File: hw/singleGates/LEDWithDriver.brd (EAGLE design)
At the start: 3 parts, among them Q1 BC817

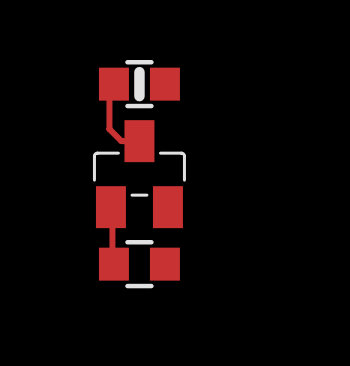
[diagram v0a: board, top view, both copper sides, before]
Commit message: Add led output and prepare first alu slice
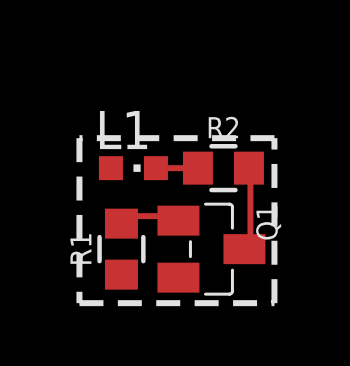
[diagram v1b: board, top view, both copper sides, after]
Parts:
- added L1: (no value), p.peter-leds:CHIPLED_0603
- R2: device p.peter-rcl:R0603-MARK -> p.peter-gator:R0603
- moved R2 3.96 mm to (4.80, 4.50), turned to 0 degrees
- moved Q1 3.47 mm to (4.40, 1.80), turned to 270 degrees
- moved R1 0.78 mm to (1.40, 1.80), turned to 90 degrees
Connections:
- net NOT renamed N$1
- new net INT: L1.C, R2.1
- net _VP: now also L1.A; no longer R2.1
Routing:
- net INT: track 0.00 -> 1.40 mm
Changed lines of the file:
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@@
 <layer number="23" name="tOrigins" color="15" fill="1" visible="yes" active="yes"/>
 <layer number="24" name="bOrigins" color="15" fill="1" visible="yes" active="yes"/>
-<layer number="25" name="tNames" color="7" fill="1" visible="yes" active="yes"/>
+<layer number="25" name="tNames" color="7" fill="1" visible="no" active="yes"/>
 <layer number="26" name="bNames" color="7" fill="1" visible="yes" active="yes"/>
-<layer number="27" name="tValues" color="7" fill="1" visible="yes" active="yes"/>
+<layer number="27" name="tValues" color="7" fill="1" visible="no" active="yes"/>
 <layer number="28" name="bValues" color="7" fill="1" visible="yes" active="yes"/>
 <layer number="29" name="tStop" color="7" fill="3" visible="yes" active="yes"/>
@@
 <layer number="107" name="Crop" color="7" fill="1" visible="yes" active="yes"/>
 <layer number="108" name="centerline" color="7" fill="1" visible="yes" active="yes"/>
-<layer number="109" name="fp9" color="7" fill="1" visible="yes" active="yes"/>
-<layer number="110" name="fp0" color="7" fill="1" visible="yes" active="yes"/>
+<layer number="109" name="fp9" color="7" fill="1" visible="no" active="yes"/>
+<layer number="110" name="fp0" color="7" fill="1" visible="no" active="yes"/>
 <layer number="116" name="Patch_BOT" color="9" fill="4" visible="yes" active="yes"/>
 <layer number="121" name="_tsilk" color="7" fill="1" visible="yes" active="yes"/>
 <layer number="122" name="_bsilk" color="7" fill="1" visible="yes" active="yes"/>
-<layer number="123" name="tTestmark" color="7" fill="1" visible="yes" active="yes"/>
-<layer number="124" name="bTestmark" color="7" fill="1" visible="yes" active="yes"/>
+<layer number="123" name="tTestmark" color="7" fill="1" visible="no" active="yes"/>
+<layer number="124" name="bTestmark" color="7" fill="1" visible="no" active="yes"/>
 <layer number="125" name="_tNames" color="7" fill="1" visible="yes" active="yes"/>
 <layer number="131" name="prix" color="7" fill="1" visible="yes" active="yes"/>
@@
 <layer number="144" name="Drill_legend" color="7" fill="1" visible="yes" active="yes"/>
 <layer number="151" name="HeatSink" color="7" fill="1" visible="yes" active="yes"/>
-<layer number="199" name="Contour" color="7" fill="1" visible="yes" active="yes"/>
+<layer number="199" name="Contour" color="7" fill="1" visible="no" active="yes"/>
 <layer number="200" name="200bmp" color="1" fill="10" visible="no" active="no"/>
 <layer number="201" name="201bmp" color="2" fill="10" visible="yes" active="yes"/>
@@
 <board>
 <plain>
-<wire x1="0" y1="8.5" x2="4" y2="8.5" width="0.2" layer="22" style="shortdash"/>
-<wire x1="4" y1="8.5" x2="4" y2="0" width="0.2" layer="22" style="shortdash"/>
-<wire x1="4" y1="0" x2="0" y2="0" width="0.2" layer="22" style="shortdash"/>
-<wire x1="0" y1="0" x2="0" y2="8.5" width="0.2" layer="22" style="shortdash"/>
+<wire x1="0" y1="0" x2="6.5" y2="0" width="0.2" layer="21" style="shortdash"/>
+<wire x1="6.5" y1="0" x2="6.5" y2="5.5" width="0.2" layer="21" style="shortdash"/>
+<wire x1="6.5" y1="5.5" x2="0" y2="5.5" width="0.2" layer="21" style="shortdash"/>
+<wire x1="0" y1="5.5" x2="0" y2="0" width="0.2" layer="21" style="shortdash"/>
 </plain>
 <attributes>
@@
 </autorouter>
 <elements>
-<element name="R1" library="p.peter-gator" package="R0603" value="10k" x="2" y="1.3" smashed="yes" rot="R180">
-<attribute name="SV_SPICE_ORDER" value="1;2" x="2" y="1.3" size="1.778" layer="27" rot="R180" display="off"/>
-<attribute name="SV_SPICE_PREFIX" value="R" x="2" y="1.3" size="1.778" layer="27" rot="R180" display="off"/>
+<element name="R1" library="p.peter-gator" package="R0603" value="10k" x="1.4" y="1.8" rot="R90">
+<attribute name="SV_SPICE_ORDER" value="1;2" x="1.4" y="1.8" size="1.778" layer="27" rot="R90" display="off"/>
+<attribute name="SV_SPICE_PREFIX" value="R" x="1.4" y="1.8" size="1.778" layer="27" rot="R90" display="off"/>
 </element>
-<element name="R2" library="p.peter-rcl" package="R0603-MARK" value="1k" x="2" y="7.3" smashed="yes" rot="R180"/>
-<element name="Q1" library="p.peter-gator" package="SOT23" value="BC817" x="2" y="4.3" smashed="yes">
-<attribute name="SV_SPICE_MODEL" value="NPN ()" x="2" y="4.3" size="1.778" layer="27" display="off"/>
-<attribute name="SV_SPICE_ORDER" value="COLLECTOR;BASE;EMITTER" x="2" y="4.3" size="1.778" layer="27" display="off"/>
-<attribute name="SV_SPICE_PREFIX" value="Q" x="2" y="4.3" size="1.778" layer="27" display="off"/>
+<element name="R2" library="p.peter-gator" package="R0603" value="1k" x="4.8" y="4.5">
+<attribute name="SV_SPICE_ORDER" value="1;2" x="4.8" y="4.5" size="1.778" layer="27" display="off"/>
+<attribute name="SV_SPICE_PREFIX" value="R" x="4.8" y="4.5" size="1.778" layer="27" display="off"/>
 </element>
+<element name="Q1" library="p.peter-gator" package="SOT23" value="BC817" x="4.4" y="1.8" rot="R270">
+<attribute name="SV_SPICE_MODEL" value="NPN ()" x="4.4" y="1.8" size="1.778" layer="27" rot="R270" display="off"/>
+<attribute name="SV_SPICE_ORDER" value="COLLECTOR;BASE;EMITTER" x="4.4" y="1.8" size="1.778" layer="27" rot="R270" display="off"/>
+<attribute name="SV_SPICE_PREFIX" value="Q" x="4.4" y="1.8" size="1.778" layer="27" rot="R270" display="off"/>
+</element>
+<element name="L1" library="p.peter-leds" package="CHIPLED_0603" value="" x="1.8" y="4.5" rot="R270"/>
 </elements>
 <signals>
 <signal name="_VN">
+<wire x1="3.5" y1="0.65" x2="3.3" y2="0.85" width="0.2" layer="1"/>
 <contactref element="Q1" pad="P$2"/>
 </signal>
-<signal name="N$14">
+<signal name="INT">
+<contactref element="R2" pad="1"/>
+<contactref element="L1" pad="C"/>
+<wire x1="3.95" y1="4.5" x2="2.55" y2="4.5" width="0.2" layer="1"/>
+</signal>
+<signal name="N$16">
 <contactref element="R1" pad="2"/>
-<wire x1="1.15" y1="1.3" x2="1.15" y2="1.35" width="0.2" layer="1"/>
-<wire x1="1.15" y1="1.35" x2="1.1" y2="1.4" width="0.2" layer="1"/>
-<wire x1="1.1" y1="1.4" x2="1.1" y2="3.15" width="0.2" layer="1"/>
-<wire x1="1.1" y1="3.15" x2="1.05" y2="3.2" width="0.2" layer="1"/>
+<wire x1="1.4" y1="2.65" x2="1.4" y2="2.8" width="0.2" layer="1"/>
+<wire x1="1.4" y1="2.8" x2="1.4" y2="2.9" width="0.2" layer="1"/>
+<wire x1="1.4" y1="2.9" x2="3.25" y2="2.9" width="0.2" layer="1"/>
+<wire x1="3.25" y1="2.9" x2="3.3" y2="2.75" width="0.2" layer="1"/>
 <contactref element="Q1" pad="P$1"/>
-</signal>
-<signal name="NOT">
-<contactref element="R2" pad="2"/>
-<wire x1="1" y1="7.3" x2="1" y2="8.5" width="0" layer="19" extent="1-16"/>
-<wire x1="1.15" y1="7.3" x2="1" y2="7.3" width="0.2" layer="1"/>
-<wire x1="1" y1="7.3" x2="1" y2="5.8" width="0.2" layer="1"/>
-<wire x1="1" y1="5.8" x2="1.4" y2="5.4" width="0.2" layer="1"/>
-<wire x1="1.4" y1="5.4" x2="2" y2="5.4" width="0.2" layer="1"/>
-<contactref element="Q1" pad="P$3"/>
 </signal>
 <signal name="A">
 <contactref element="R1" pad="1"/>
+<wire x1="1.5" y1="1" x2="1.45" y2="1.05" width="0.2" layer="1"/>
+<wire x1="1.45" y1="1.05" x2="1.4" y2="0.95" width="0.2" layer="1"/>
+</signal>
+<signal name="N$1">
+<contactref element="Q1" pad="P$3"/>
+<contactref element="R2" pad="2"/>
+<wire x1="5.5" y1="1.8" x2="5.7" y2="1.8" width="0.2" layer="1"/>
+<wire x1="5.7" y1="1.8" x2="5.7" y2="4.45" width="0.2" layer="1"/>
+<wire x1="5.7" y1="4.45" x2="5.65" y2="4.5" width="0.2" layer="1"/>
 </signal>
 <signal name="_VP">
-<contactref element="R2" pad="1"/>
+<contactref element="L1" pad="A"/>
 </signal>
 </signals>
